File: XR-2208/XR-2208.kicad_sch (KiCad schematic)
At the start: 8 parts, among them IC1 XR-2208, J1 V_x, J2 V_y, J3 V_z, SW1 SW_DPDT_x2

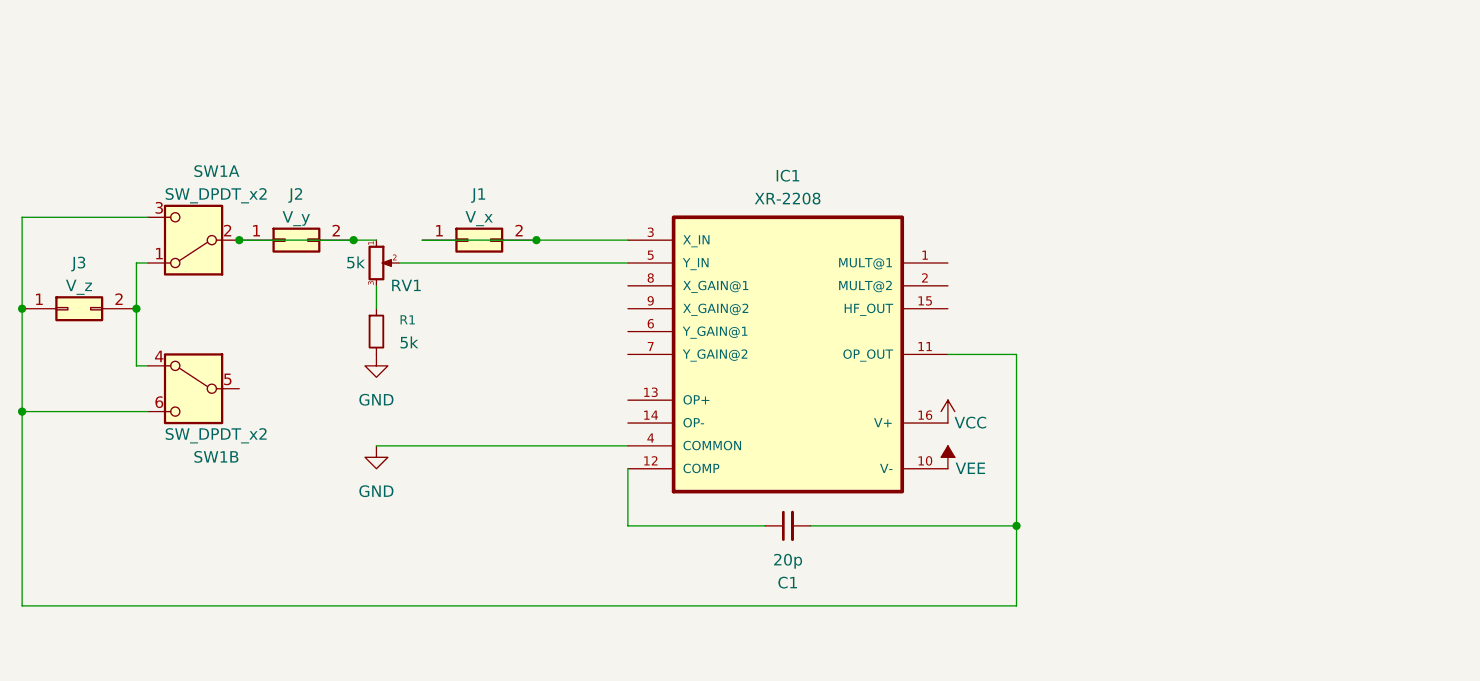
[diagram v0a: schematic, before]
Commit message: thicker 0.8mm lines
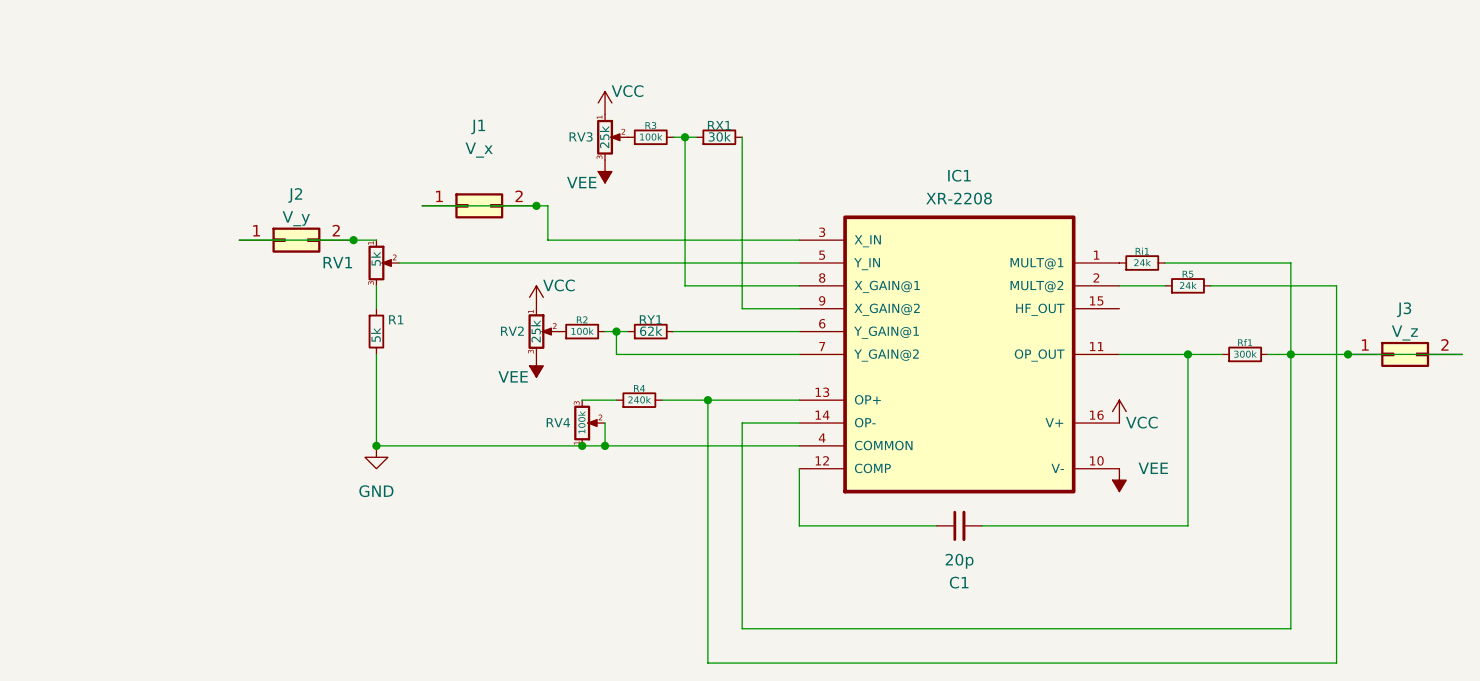
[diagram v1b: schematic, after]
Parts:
- removed SW1: SW_DPDT_x2, Button_Switch_THT:SW_CK_JS202011CQN_DPDT_Straight, symbol Switch:SW_DPDT_x2
- added R2, R3: 100k, Resistor_THT:R_Axial_DIN0207_L6.3mm_D2.5mm_P10.16mm_Horizontal, symbol Device:R_Small
- added R4: 240k, Resistor_THT:R_Axial_DIN0207_L6.3mm_D2.5mm_P10.16mm_Horizontal, symbol Device:R_Small
- added R5, Ri1: 24k, Resistor_THT:R_Axial_DIN0207_L6.3mm_D2.5mm_P10.16mm_Horizontal, symbol Device:R_Small
- added RV2, RV3: 25k, Potentiometer_THT:Potentiometer_Bourns_3296W_Vertical, symbol Device:R_Potentiometer_Small
- added RV4: 100k, Potentiometer_THT:Potentiometer_Bourns_3296W_Vertical, symbol Device:R_Potentiometer_Small
- added RX1: 30k, Resistor_THT:R_Axial_DIN0207_L6.3mm_D2.5mm_P10.16mm_Horizontal, symbol Device:R_Small
- added RY1: 62k, Resistor_THT:R_Axial_DIN0207_L6.3mm_D2.5mm_P10.16mm_Horizontal, symbol Device:R_Small
- added Rf1: 300k, Resistor_THT:R_Axial_DIN0207_L6.3mm_D2.5mm_P10.16mm_Horizontal, symbol Device:R_Small
- C1: footprint (none) -> Capacitor_THT:C_Disc_D3.0mm_W1.6mm_P2.50mm
- R1: footprint (none) -> Resistor_THT:R_Axial_DIN0207_L6.3mm_D2.5mm_P10.16mm_Horizontal
- RV1: footprint Potentiometer_THT:Potentiometer_Alpha_RD901F-40-00D_Single_Vertical -> Potentiometer_THT:Potentiometer_Bourns_3296W_Vertical
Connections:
- net GND: now also RV4.1, RV4.2
- net VCC: now also RV2.1, RV3.1
- net VEE: now also RV2.3, RV3.3
- net at IC1.1 (MULT@1): now also Ri1.1
- net at C1.2, IC1.11 (OP_OUT): now also Rf1.1; no longer J3.1 (Pin_1)
- net at IC1.13 (OP+): now also R4.2, R5.2
- net at IC1.14 (OP-): now also J3.1 (Pin_1), J3.2 (Pin_2), Rf1.2, Ri1.2
- net at IC1.2 (MULT@2): now also R5.1
- net at IC1.6 (Y_GAIN@1): now also RY1.2
- net at IC1.7 (Y_GAIN@2): now also R2.2, RY1.1
- net at IC1.8 (X_GAIN@1): now also R3.2, RX1.1
- net at IC1.9 (X_GAIN@2): now also RX1.2
- new net: R2.1, RV2.2
- new net: R4.1, RV4.3
- new net: R3.1, RV3.2
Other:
- moved on the sheet: C1, IC1, J1, J3

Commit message: fix board
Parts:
- added J4: VCC, Connector_PinHeader_2.54mm:PinHeader_2x01_P2.54mm_Vertical, symbol Connector_Generic:Conn_02x01
- added J5: GND, Connector_PinHeader_2.54mm:PinHeader_2x01_P2.54mm_Vertical, symbol Connector_Generic:Conn_02x01
- added J6: VEE, Connector_PinHeader_2.54mm:PinHeader_2x01_P2.54mm_Vertical, symbol Connector_Generic:Conn_02x01
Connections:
- net GND: now also J5.1 (Pin_1), J5.2 (Pin_2)
- net VCC: now also J4.1 (Pin_1), J4.2 (Pin_2)
- net VEE: now also J6.1 (Pin_1), J6.2 (Pin_2)
